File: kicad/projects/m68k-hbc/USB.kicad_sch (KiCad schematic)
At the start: 22 parts, among them J20 USB_A, U22 SL811HST-AXC, U23 USB6B1, U24 MAX1562ESA+, Y7 48M

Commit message: Some Updates
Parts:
- C126: renamed from C120; value 1u -> C; footprint Capacitor_SMD:C_1206_3216Metric_Pad1.33x1.80mm_HandSolder -> Capacitor_SMD:C_0603_1608Metric_Pad1.08x0.95mm_HandSolder
- C127: renamed from C121; value 4.7u -> C; footprint Capacitor_SMD:C_1206_3216Metric_Pad1.33x1.80mm_HandSolder -> Capacitor_SMD:C_0603_1608Metric_Pad1.08x0.95mm_HandSolder
- C128: renamed from C122; value 10p -> C; footprint Capacitor_SMD:C_1206_3216Metric_Pad1.33x1.80mm_HandSolder -> Capacitor_SMD:C_0603_1608Metric_Pad1.08x0.95mm_HandSolder
- C129: renamed from C123; value 22p -> C; footprint Capacitor_SMD:C_1206_3216Metric_Pad1.33x1.80mm_HandSolder -> Capacitor_SMD:C_0603_1608Metric_Pad1.08x0.95mm_HandSolder
- C130: renamed from C124; value 22p -> C; footprint Capacitor_SMD:C_1206_3216Metric_Pad1.33x1.80mm_HandSolder -> Capacitor_SMD:C_0603_1608Metric_Pad1.08x0.95mm_HandSolder
- C14, C15, C16: value 100n -> C; footprint Capacitor_SMD:C_1206_3216Metric_Pad1.33x1.80mm_HandSolder -> Capacitor_SMD:C_0603_1608Metric_Pad1.08x0.95mm_HandSolder
- L7: renamed from L8; value 2.2u -> L
- R31: renamed from R33; value 24 -> R; footprint Resistor_SMD:R_1206_3216Metric_Pad1.30x1.75mm_HandSolder -> Resistor_SMD:R_0603_1608Metric_Pad0.98x0.95mm_HandSolder
- R32: renamed from R34; value 24 -> R; footprint Resistor_SMD:R_1206_3216Metric_Pad1.30x1.75mm_HandSolder -> Resistor_SMD:R_0603_1608Metric_Pad0.98x0.95mm_HandSolder
- R33: renamed from R35; value 15k -> R; footprint Resistor_SMD:R_1206_3216Metric_Pad1.30x1.75mm_HandSolder -> Resistor_SMD:R_0603_1608Metric_Pad0.98x0.95mm_HandSolder
- R34: renamed from R36; value 15k -> R; footprint Resistor_SMD:R_1206_3216Metric_Pad1.30x1.75mm_HandSolder -> Resistor_SMD:R_0603_1608Metric_Pad0.98x0.95mm_HandSolder
- R35: renamed from R37; value 1M -> R; footprint Resistor_SMD:R_1206_3216Metric_Pad1.30x1.75mm_HandSolder -> Resistor_SMD:R_0603_1608Metric_Pad0.98x0.95mm_HandSolder
- R36: renamed from R38; value 100 -> R; footprint Resistor_SMD:R_1206_3216Metric_Pad1.30x1.75mm_HandSolder -> Resistor_SMD:R_0603_1608Metric_Pad0.98x0.95mm_HandSolder
- R37: renamed from R39; value 100k -> R; footprint Resistor_SMD:R_1206_3216Metric_Pad1.30x1.75mm_HandSolder -> Resistor_SMD:R_0603_1608Metric_Pad0.98x0.95mm_HandSolder
- R38: renamed from R40; value 470k -> R; footprint Resistor_SMD:R_1206_3216Metric_Pad1.30x1.75mm_HandSolder -> Resistor_SMD:R_0603_1608Metric_Pad0.98x0.95mm_HandSolder
- U28: renamed from U24; footprint Package_SO:SOIC-8_3.9x4.9mm_P1.27mm -> MAX1562ESA+:SOIC127P600X175-8N
- Y7: value 48M -> Crystal
- renumbered J20 to J18, U22 to U26, U23 to U27
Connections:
- net A0 renamed OPB_A0
- net D24 renamed OPB_D0
- net D25 renamed OPB_D1
- net D26 renamed OPB_D2
- net D27 renamed OPB_D3
- net D28 renamed OPB_D4
- net D29 renamed OPB_D5
- net D30 renamed OPB_D6
- net D31 renamed OPB_D7
- net USBIRQ renamed IRQ_USBC
- net ~{PERRST} renamed ~{RST_USBC}
- net ~{RD} renamed ~{OPB_RD}
- net ~{USBCS} renamed ~{CS_USBC}
- net ~{WR} renamed ~{OPB_WR}
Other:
- note added: "OPB Signals"

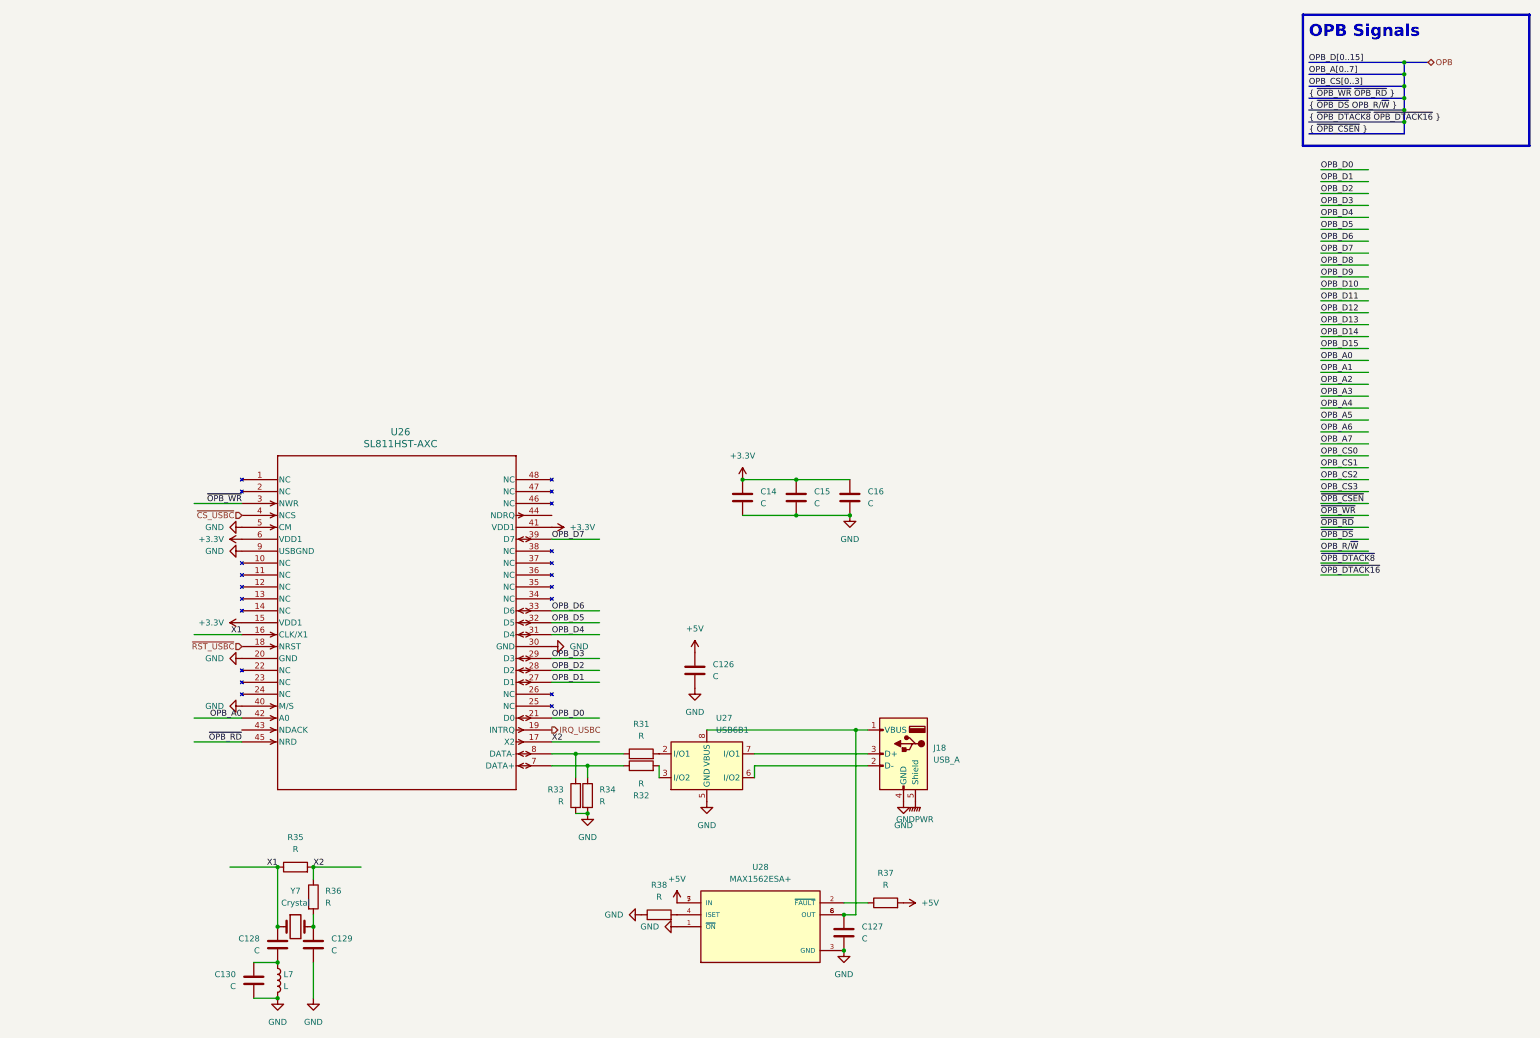
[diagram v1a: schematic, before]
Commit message: Large changes: EHBCSimpleEmu, kicad, fwcode, docs
This commit contains some large changes:
- Removed EHBCSimpleEmu (Moved to kms1212/llemu, kms1212/qemu)
- (likely) Removed fwcode; now it only boots and stops
- Modified documents
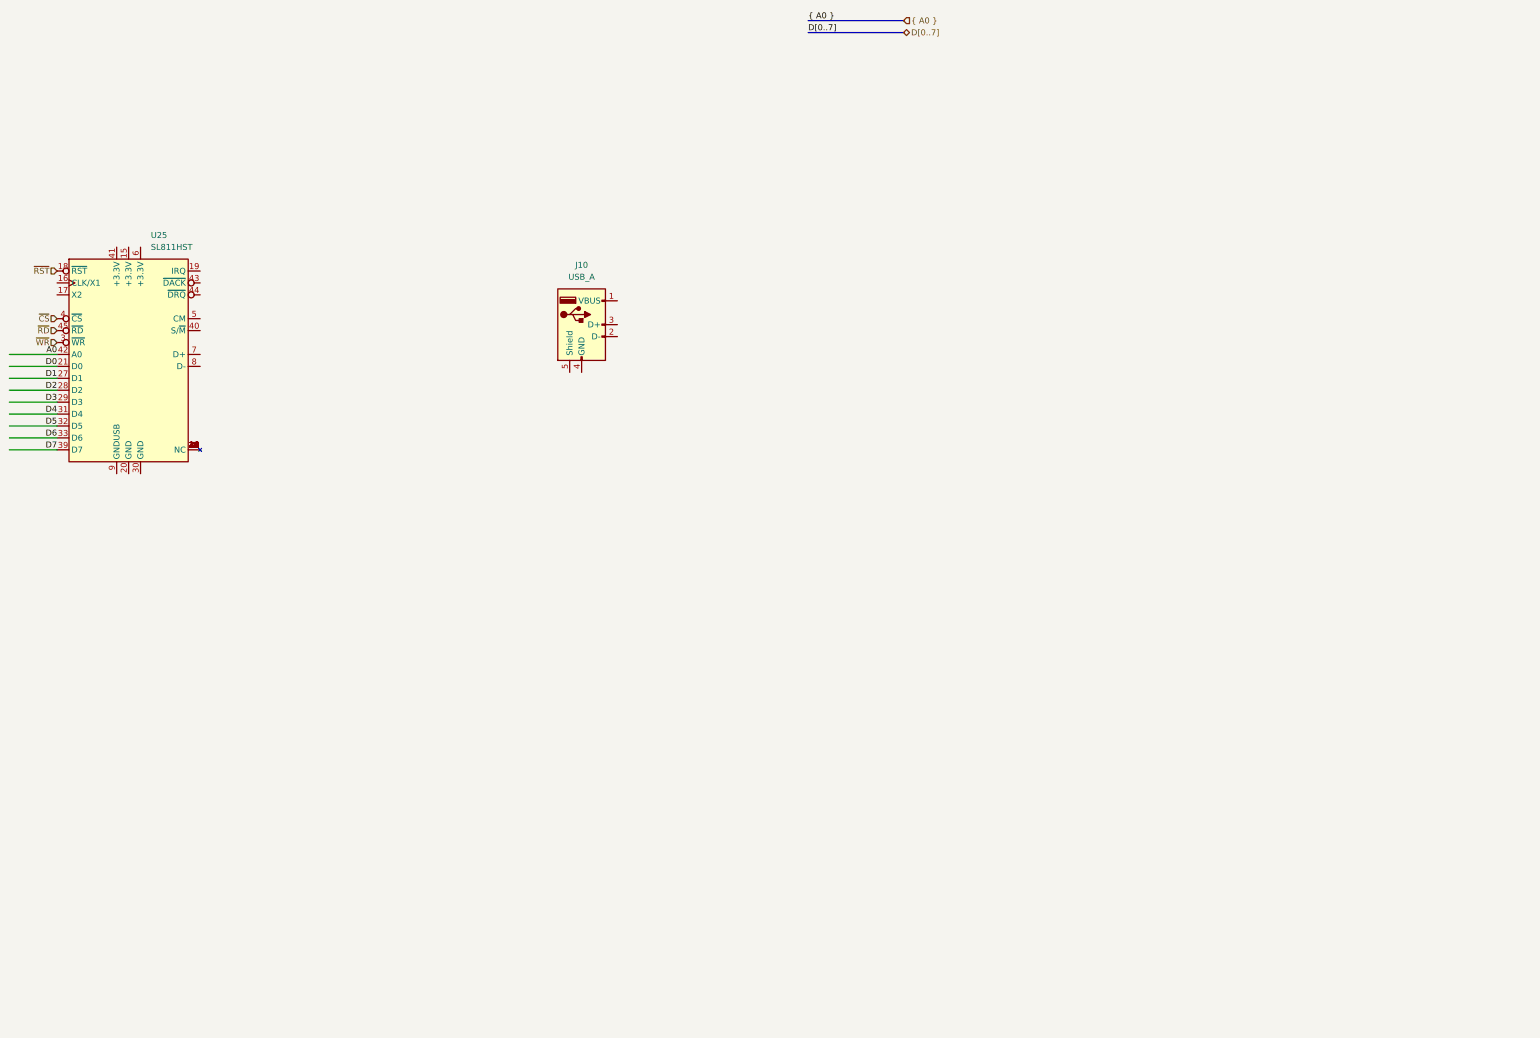
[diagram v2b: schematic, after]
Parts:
- removed C126, C127, C128, C129, C130, C14, C15, C16: C, Capacitor_SMD:C_0603_1608Metric_Pad1.08x0.95mm_HandSolder, symbol Device:C
- removed J18: USB_A, Connector_USB:USB_A_Wuerth_614004134726_Horizontal, symbol Connector:USB_A
- removed L7: L, Inductor_SMD:L_1206_3216Metric_Pad1.42x1.75mm_HandSolder, symbol Device:L
- removed R31, R32, R33, R34, R35, R36, R37, R38: R, Resistor_SMD:R_0603_1608Metric_Pad0.98x0.95mm_HandSolder, symbol Device:R
- removed U26: SL811HST-AXC, Package_QFP:TQFP-48_7x7mm_P0.5mm, symbol SL811HST-AXC:SL811HST-AXC
- removed U27: USB6B1, Package_SO:SOIC-8_3.9x4.9mm_P1.27mm, symbol Power_Protection:USB6B1
- removed U28: MAX1562ESA+, MAX1562ESA+:SOIC127P600X175-8N, symbol MAX1562ESA:MAX1562ESA+
- removed Y7: Crystal, Crystal:Crystal_HC52-6mm_Vertical, symbol Device:Crystal
- added J10: USB_A, Connector_USB:USB_A_Wuerth_614004134726_Horizontal, symbol Connector:USB_A
- added U25: SL811HST, Package_QFP:TQFP-48_7x7mm_P0.5mm, symbol m68k-hbc-ic:SL811HST
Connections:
- new net: U25.1 (NC), U25.10 (NC), U25.11 (NC), U25.12 (NC), U25.13 (NC), U25.14 (NC), U25.2 (NC), U25.22 (NC), U25.23 (NC), U25.24 (NC), U25.25 (NC), U25.26 (NC), U25.34 (NC), U25.35 (NC), U25.36 (NC), U25.37 (NC), U25.38 (NC), U25.46 (NC), U25.47 (NC), U25.48 (NC)
- new net A0: U25.42 (A0)
- new net D0: U25.21 (D0)
- new net D1: U25.27 (D1)
- new net D2: U25.28 (D2)
- new net D3: U25.29 (D3)
- new net D4: U25.31 (D4)
- new net D5: U25.32 (D5)
- new net D6: U25.33 (D6)
- new net D7: U25.39 (D7)
- new net ~{CS}: U25.4 (~{CS})
- new net ~{RD}: U25.45 (~{RD})
- new net ~{RST}: U25.18 (~{RST})
- new net ~{WR}: U25.3 (~{WR})
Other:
- note removed: "OPB Signals"
